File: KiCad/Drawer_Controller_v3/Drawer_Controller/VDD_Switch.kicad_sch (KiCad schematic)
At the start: 5 parts, among them Q7 AO3400A, Q8 AO3401A

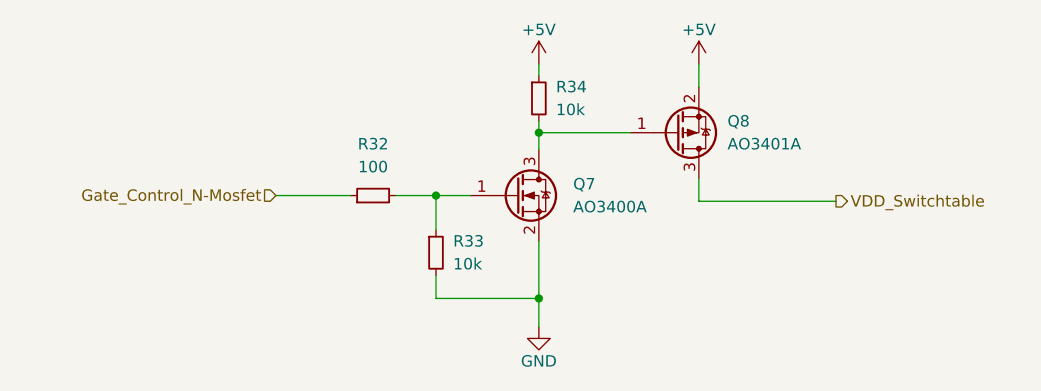
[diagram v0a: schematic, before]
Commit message: Progress in updating schematic for v3 - WIP
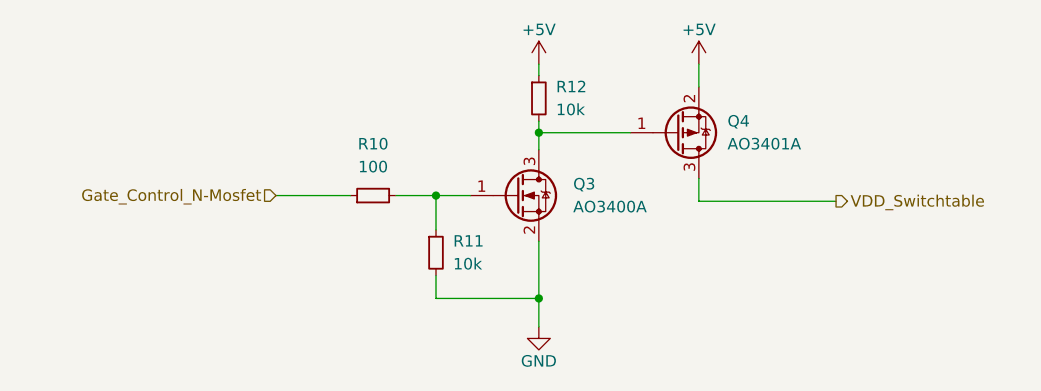
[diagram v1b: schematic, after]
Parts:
- renumbered Q7 to Q3, Q8 to Q4, R32 to R10, R33 to R11, R34 to R12

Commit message: Finished assigning all footprints
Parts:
- R10, R11, R12: footprint Resistor_SMD:R_0805_2012Metric_Pad1.20x1.40mm_HandSolder -> Capacitor_SMD:C_0603_1608Metric
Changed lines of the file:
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@@
       (effects (font (size 1.27 1.27)))
     )
-    (property "Footprint" "Resistor_SMD:R_0805_2012Metric_Pad1.20x1.40mm_HandSolder" (at 106.045 85.725 0)
+    (property "Footprint" "Capacitor_SMD:C_0603_1608Metric" (at 106.045 85.725 0)
       (effects (font (size 1.27 1.27)) hide)
     )
@@
       (effects (font (size 1.27 1.27)) (justify left))
     )
-    (property "Footprint" "Resistor_SMD:R_0805_2012Metric_Pad1.20x1.40mm_HandSolder" (at 113.03 92.075 0)
+    (property "Footprint" "Capacitor_SMD:C_0603_1608Metric" (at 113.03 92.075 0)
       (effects (font (size 1.27 1.27)) hide)
     )
@@
       (effects (font (size 1.27 1.27)) (justify left))
     )
-    (property "Footprint" "Resistor_SMD:R_0805_2012Metric_Pad1.20x1.40mm_HandSolder" (at 124.46 74.93 0)
+    (property "Footprint" "Capacitor_SMD:C_0603_1608Metric" (at 124.46 74.93 0)
       (effects (font (size 1.27 1.27)) hide)
     )

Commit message: Starting routing the PCB - WIP
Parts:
- R11, R12: footprint Capacitor_SMD:C_0603_1608Metric -> Resistor_SMD:R_0402_1005Metric
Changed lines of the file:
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@@
       (effects (font (size 1.27 1.27)) (justify left))
     )
-    (property "Footprint" "Capacitor_SMD:C_0603_1608Metric" (at 113.03 92.075 0)
+    (property "Footprint" "Resistor_SMD:R_0402_1005Metric" (at 113.03 92.075 0)
       (effects (font (size 1.27 1.27)) hide)
     )
@@
       (effects (font (size 1.27 1.27)) (justify left))
     )
-    (property "Footprint" "Capacitor_SMD:C_0603_1608Metric" (at 124.46 74.93 0)
+    (property "Footprint" "Resistor_SMD:R_0402_1005Metric" (at 124.46 74.93 0)
       (effects (font (size 1.27 1.27)) hide)
     )

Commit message: First draft for manufacturing files
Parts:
- R10: footprint Capacitor_SMD:C_0603_1608Metric -> Resistor_SMD:R_0603_1608Metric
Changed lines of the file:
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@@
       (effects (font (size 1.27 1.27)))
     )
-    (property "Footprint" "Capacitor_SMD:C_0603_1608Metric" (at 106.045 85.725 0)
+    (property "Footprint" "Resistor_SMD:R_0603_1608Metric" (at 106.045 85.725 0)
       (effects (font (size 1.27 1.27)) hide)
     )
